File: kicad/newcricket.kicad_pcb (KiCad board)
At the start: 2 copper layers, 23 parts, among them IC11 ATTINY85-P, Q11 Q_NPN_BCE, SW11 SWITCH_INV, SW11 SW_PUSH, U11 78L05, U11 LM335

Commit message: A first version of the board and some changes to the schematic.
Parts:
- removed BT11 (x2): Battery, AAAAAGGHGGHGG:SMD_cr2032_holder
- removed C11: .01uF, Capacitors_SMD:C_1206_HandSoldering
- removed C11: 22uF, Capacitors_SMD:C_1210_HandSoldering
- removed C11: .01uF, Capacitors_SMD:C_1206
- removed D11: DIODE, Diodes_SMD:SOD-323
- removed IC11: ATTINY85-P, Housings_DIP:DIP-8_W7.62mm
- removed Q11: Q_NPN_BCE, TO_SOT_Packages_SMD:SOT-23_Handsoldering
- removed R11 (x5): 10k, Resistors_SMD:R_1206_HandSoldering
- removed R11: 1k, Resistors_SMD:R_1206_HandSoldering
- removed R11: LDR, AAAAAGGHGGHGG:LDR
- removed RV11 (x2): POT, bourns:BOURNS-3362P
- removed SP11: SPEAKER, Buzzers_Beepers:MagneticBuzzer_ProSignal_ABT-410-RC
- removed SW11 (x2): SW_PUSH, Buttons_Switches_SMD:SW_SPST_EVPBF
- removed SW11: SWITCH_INV, Buttons_Switches_SMD:SW_SPDT_PCM12
- removed U11: LM335, TO_SOT_Packages_THT:TO-92_Inline_Narrow_Oval
- removed U11: 78L05, AAAAAGGHGGHGG:78L05_handsoldering
- added BT1: Battery, aaevan_footprints:SMD_cr2032_holder, F.Cu at (91.9, 90.7)
- added BT2: Battery, aaevan_footprints:SMD_cr2032_holder, B.Cu at (91.9, 90.7)
- added C1: .01uF, Capacitors_SMD:C_1206_HandSoldering, B.Cu at (90.2, 76.0)
- added C2: 22uF, Capacitors_SMD:C_1210_HandSoldering, B.Cu at (87.3, 105.9)
- added C3: .01uF, Capacitors_SMD:C_1206_HandSoldering, B.Cu at (91.6, 69.0)
- added D1: DIODE, aaevan_footprints:SOD-323_handsoldering, B.Cu at (94.6, 108.5)
- added D2: D, aaevan_footprints:SOD-323_handsoldering, B.Cu at (99.9, 106.8)
- added D3: D, aaevan_footprints:SOD-323_handsoldering, B.Cu at (99.9, 110.9)
- added IC1: ATTINY85-P, Housings_DIP:DIP-8_W7.62mm, F.Cu at (87.8, 68.0)
- added Q1: Q_NPN_BCE, TO_SOT_Packages_SMD:SOT-23_Handsoldering, B.Cu at (94.6, 103.4)
- added R1: 10k, Resistors_SMD:R_1206_HandSoldering, B.Cu at (100.0, 75.3)
- added R2: 10k, Resistors_SMD:R_1206_HandSoldering, B.Cu at (83.2, 70.8)
- added R3: 10k, Resistors_SMD:R_1206_HandSoldering, B.Cu at (100.0, 71.0)
- added R4: 1k, Resistors_SMD:R_1206_HandSoldering, B.Cu at (83.2, 76.2)
- added R5: 10k, Resistors_SMD:R_1206_HandSoldering, B.Cu at (83.2, 73.5)
- added R6: LDR, aaevan_footprints:LDR, F.Cu at (104.1, 94.6)
- added R7: 10k, Resistors_SMD:R_1206_HandSoldering, B.Cu at (83.2, 68.1)
- added R8: JMP, Resistors_SMD:R_1206_HandSoldering, B.Cu at (95.0, 111.0)
- added RV1: POT, bourns:BOURNS-3362P, F.Cu at (101.2, 100.8)
- added RV2: POT, bourns:BOURNS-3362P, F.Cu at (82.1, 81.0)
- added SP1: SPEAKER, Buzzers_Beepers:MagneticBuzzer_ProSignal_ABT-410-RC, F.Cu at (97.8, 108.5)
- added SW1: SW_PUSH, Buttons_Switches_SMD:SW_SPST_EVPBF, F.Cu at (100.1, 71.9)
- added SW2: SW_PUSH, Buttons_Switches_SMD:SW_SPST_EVPBF, F.Cu at (85.1, 107.8)
- added SW3: SWITCH_INV, Buttons_Switches_SMD:SW_SPDT_PCM12, F.Cu at (103.7, 108.7)
- added U1: LM335, TO_SOT_Packages_THT:TO-92_Inline_Narrow_Oval, F.Cu at (80.6, 87.8)

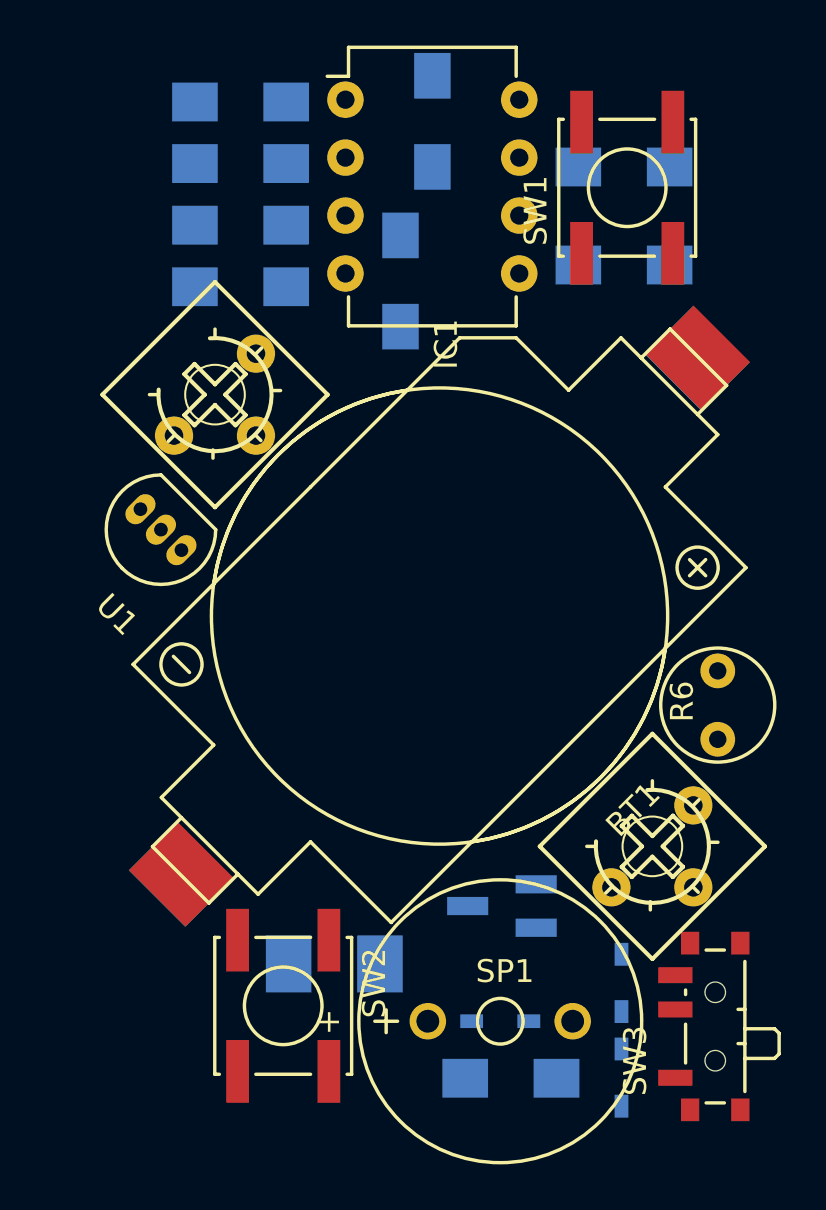
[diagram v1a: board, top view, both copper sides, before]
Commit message: Rearranged some components, soon to start laying traces.
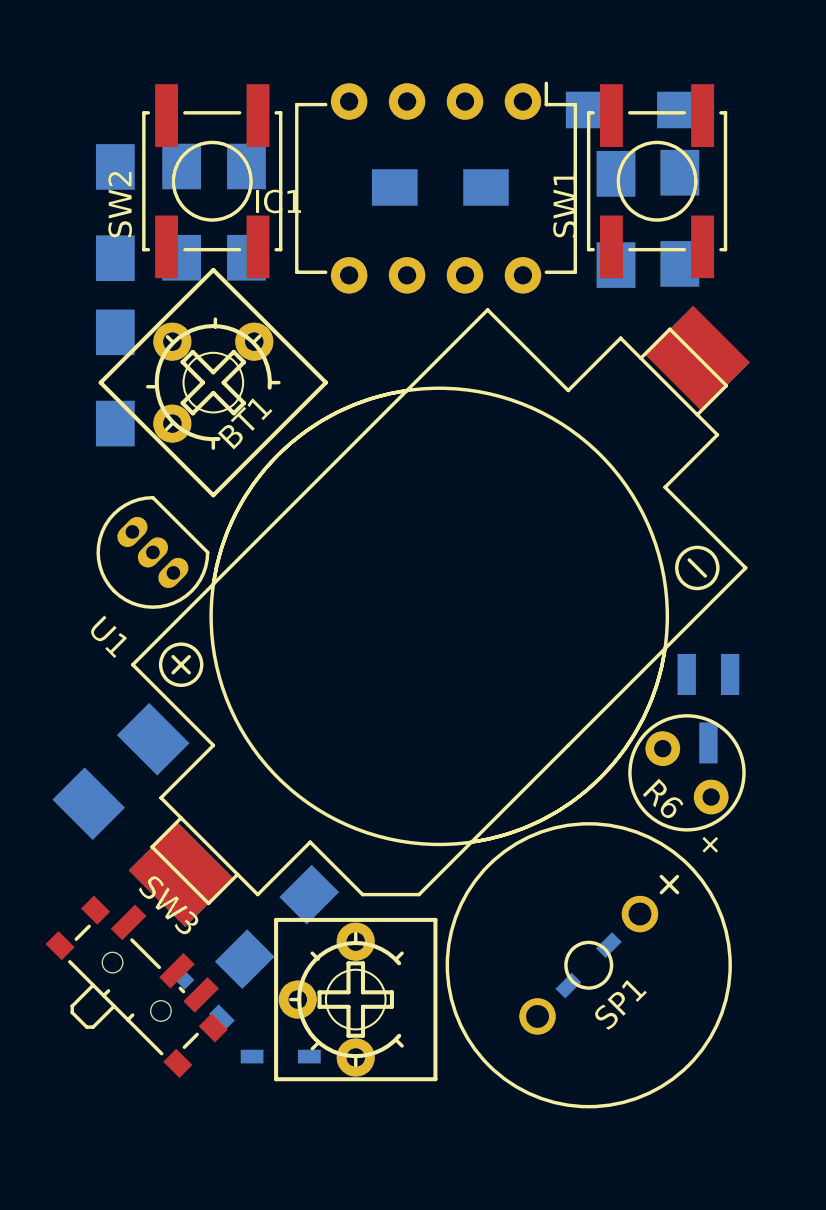
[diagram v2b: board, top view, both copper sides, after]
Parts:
- moved SW2 36.3 mm to (82.0, 71.6), turned to 90 degrees
- moved SW3 24.9 mm to (78.9, 106.7), turned to 315 degrees
- moved D2 18.4 mm to (81.5, 107.4), turned to 135 degrees
- moved D3 15.0 mm to (85.0, 110.0), turned to 180 degrees
- moved RV1 14.6 mm to (88.2, 107.5), turned to 90 degrees
- moved R7 13.3 mm to (77.7, 80.2), turned to 270 degrees
- moved C1 12.7 mm to (100.5, 68.5), turned to 0 degrees
- moved C2 12.6 mm to (78.0, 97.5), turned to 45 degrees
- moved Q1 12.5 mm to (103.7, 94.7), turned to 0 degrees
- moved R8 12.2 mm to (84.8, 104.3), turned to 225 degrees
- moved IC1 7.78 mm to (95.6, 68.1), turned to 270 degrees
- moved R2 5.89 mm to (77.7, 73.0), turned to 90 degrees
- moved D1 4.58 mm to (98.5, 106.0), turned to 45 degrees
- moved R3 3.33 mm to (102.5, 73.2), turned to 90 degrees
- moved R4 3.28 mm to (83.5, 73.0), turned to 90 degrees
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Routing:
- net (no net): track 0.00 -> 1.50 mm

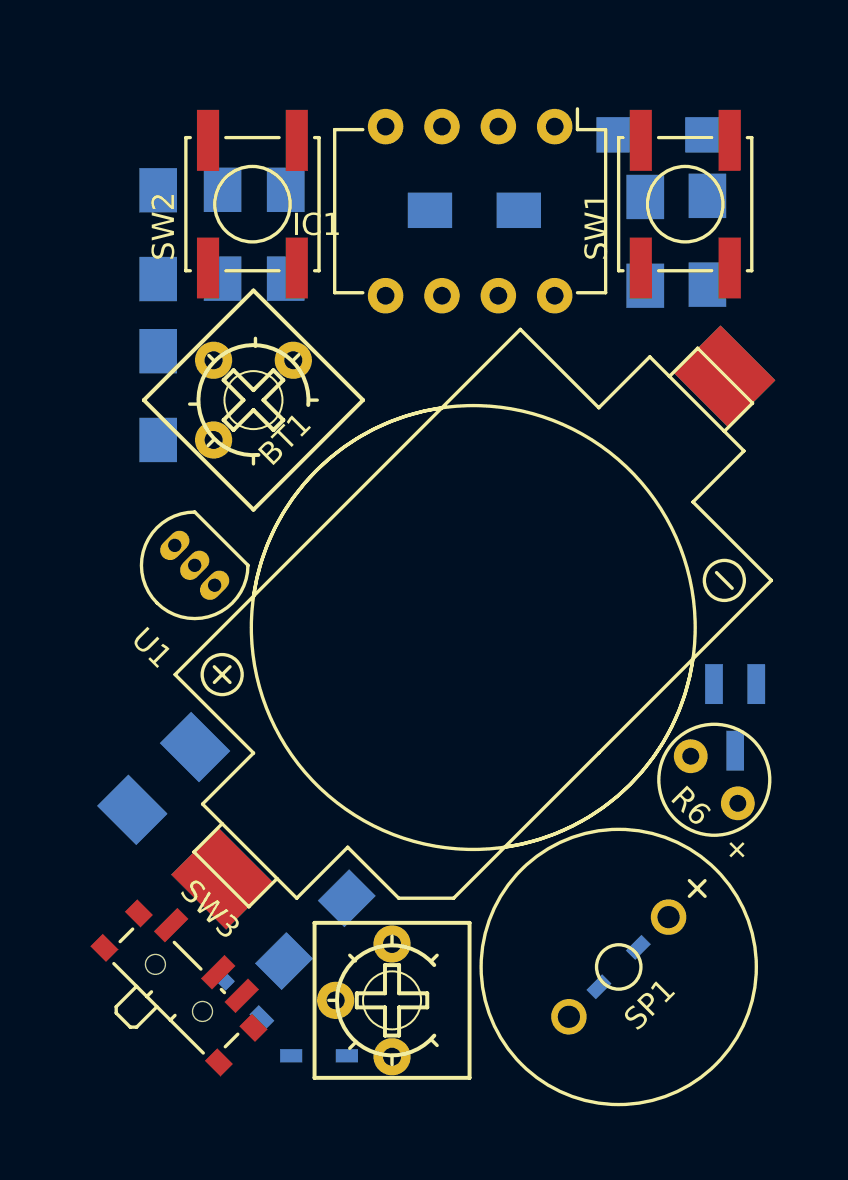
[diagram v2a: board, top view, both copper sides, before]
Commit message: Most of a layout-- still need to fix the switch so it's connected.
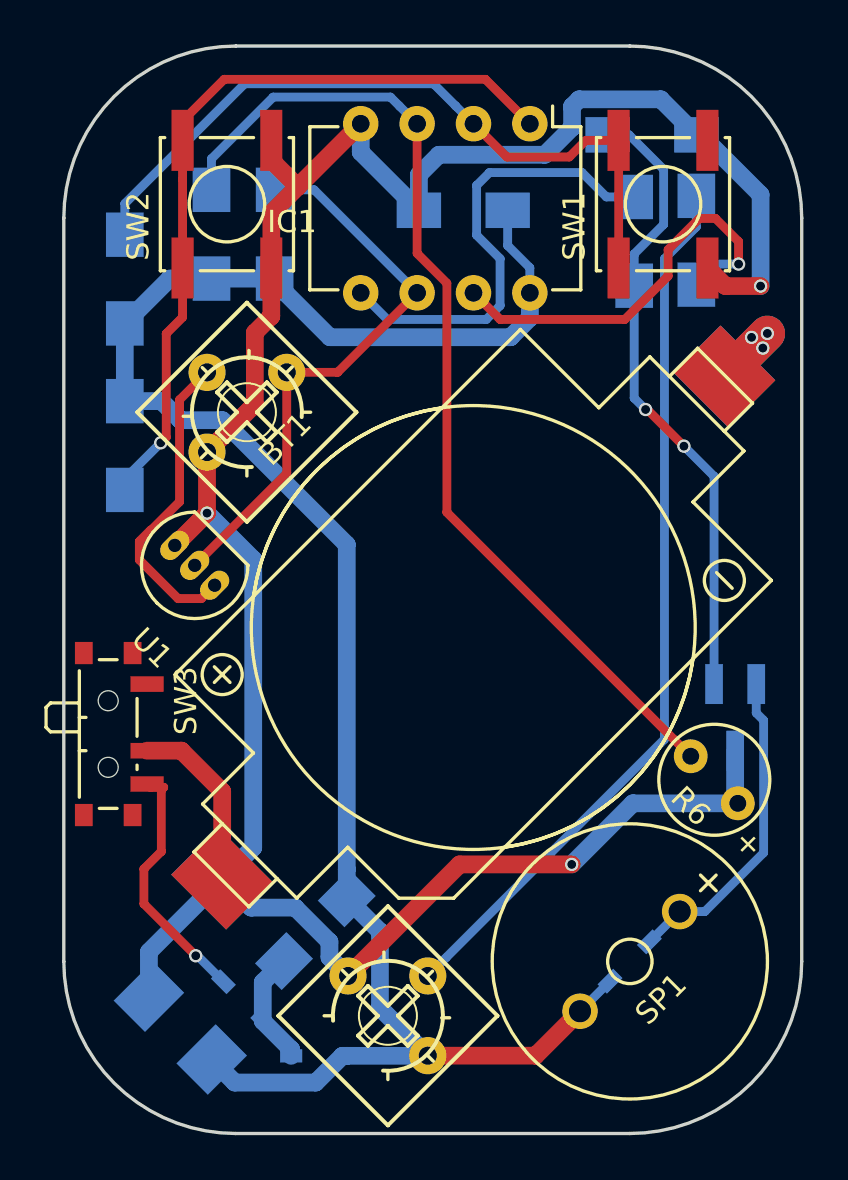
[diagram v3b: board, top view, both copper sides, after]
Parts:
- moved SW3 11.6 mm to (75.8, 95.5), turned to 270 degrees
- moved C2 11.3 mm to (78.7, 108.8), turned to 315 degrees
- moved R7 2.70 mm to (76.2, 82.5)
- moved R2 2.50 mm to (76.2, 75.0)
- moved SW2 1.15 mm to (80.8, 71.6)
- moved IC1 1.13 mm to (94.5, 68.0)
- moved SW1 1.00 mm to (100.5, 71.6)
- moved RV1 0.72 mm to (88.1, 108.2), turned to 315 degrees
- moved RV2 0.62 mm to (81.7, 81.0)
- moved D1 0.56 mm to (99.0, 105.8)
- moved SP1 0.56 mm to (96.7, 108.0)
- moved C1 0.50 mm to (100.0, 68.5)
- moved C3 0.50 mm to (91.5, 71.9)
- moved R1 0.50 mm to (99.2, 73.3)
- moved R3 0.50 mm to (102.0, 73.2)
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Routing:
- net GND: track 0.00 -> 114.2 mm, vias 0 -> 3
- net VCC: track 0.00 -> 86.9 mm
- net Net-(IC1-Pad3): track 0.00 -> 45.9 mm
- net Net-(R3-Pad2): track 0.00 -> 40.2 mm
- net Net-(IC1-Pad1): track 0.00 -> 35.0 mm, vias 0 -> 1
- net Net-(IC1-Pad2): track 0.00 -> 33.3 mm
- net Net-(C1-Pad1): track 0.00 -> 28.4 mm, vias 0 -> 2
- net Net-(IC1-Pad6): track 0.00 -> 26.1 mm
- net Net-(IC1-Pad5): track 0.00 -> 20.7 mm
- net Net-(IC1-Pad7): track 0.00 -> 18.8 mm, vias 0 -> 1
- net Net-(D1-Pad2): track 0.00 -> 14.5 mm
- net Net-(RV2-Pad2): track 0.00 -> 14.1 mm
- net Net-(D2-Pad2): track 0.00 -> 11.5 mm, vias 0 -> 1
- net Net-(BT1-Pad1): track 0.00 -> 8.07 mm
- net Net-(BT1-Pad2): track 0.00 -> 5.48 mm, vias 0 -> 1
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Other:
- board outline added: 33.2 x 49 mm

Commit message: Still throwing a few errors, filled zone placed. Board looking near-complete.
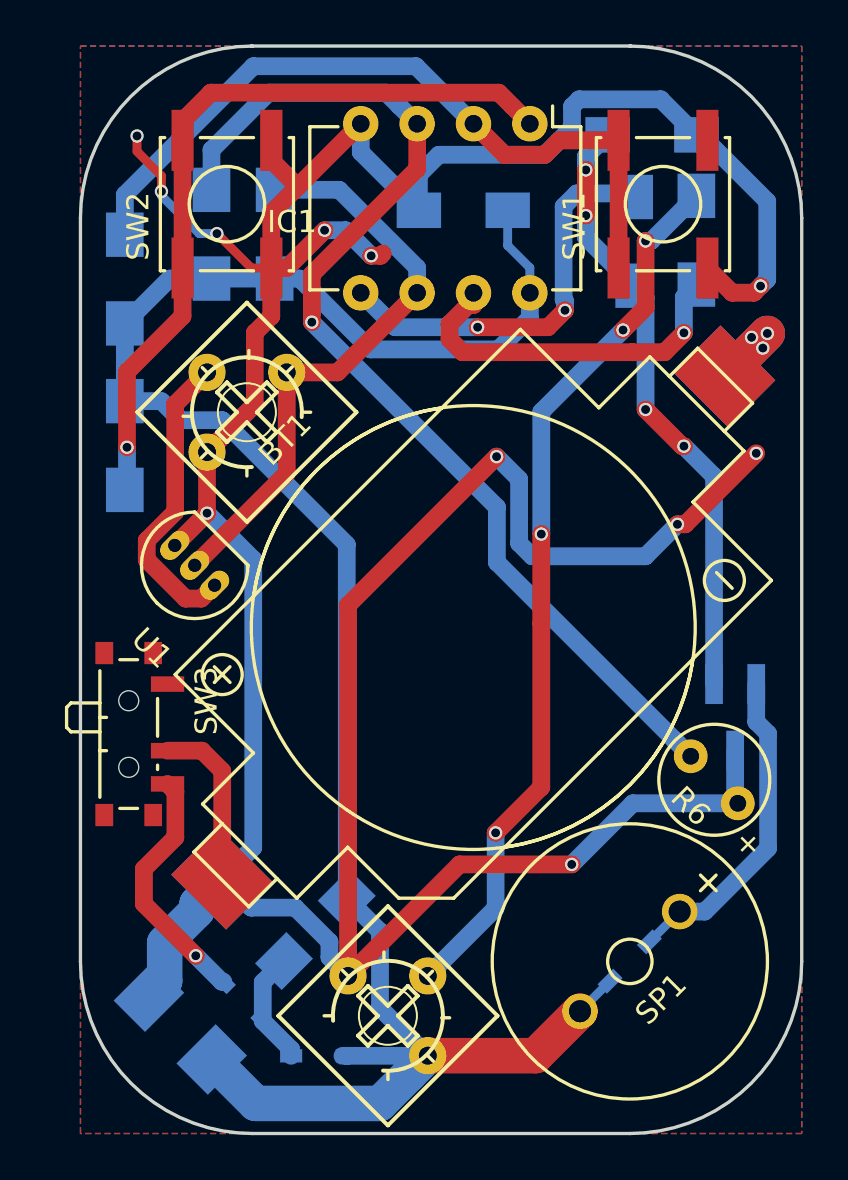
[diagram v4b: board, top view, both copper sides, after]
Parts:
- moved SW3 0.92 mm to (76.7, 95.5)
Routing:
- net GND: track 114.2 -> 173.8 mm, vias 3 -> 11
- net VCC: track 86.9 -> 91.9 mm
- net Net-(IC1-Pad3): track 45.9 -> 50.2 mm, vias 0 -> 2
- net Net-(IC1-Pad7): track 18.8 -> 16.2 mm
- net Net-(IC1-Pad1): track 35.0 -> 36.4 mm
- net Net-(R3-Pad2): track 40.2 -> 41.5 mm, vias 0 -> 4
- net Net-(C1-Pad1): track 28.4 -> 27.6 mm, vias 2 -> 4
- net Net-(IC1-Pad2): track 33.3 -> 34.1 mm
- net Net-(IC1-Pad6): track 26.1 -> 26.8 mm
- net Net-(IC1-Pad5): track 20.7 -> 20.0 mm, vias 0 -> 2
- added copper zone on B.Cu, net GND
- added copper zone on F.Cu, net GND
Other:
- board size 33.2 x 49 mm -> 32.5 x 49 mm

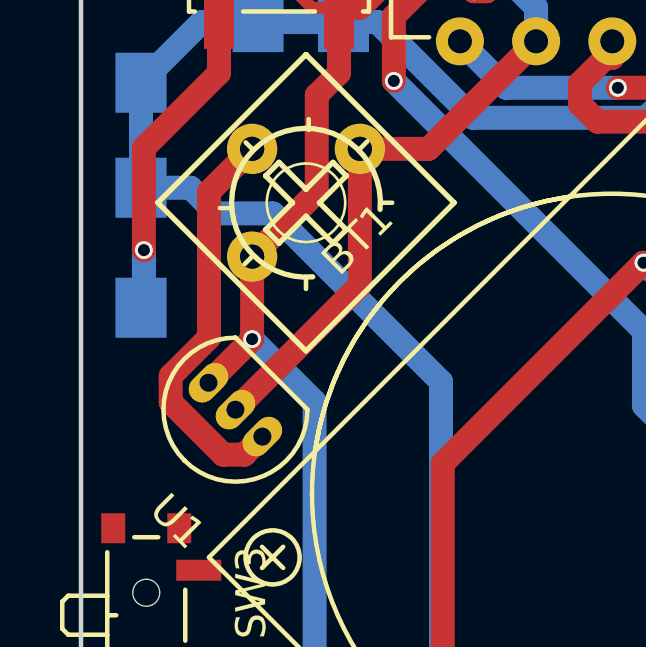
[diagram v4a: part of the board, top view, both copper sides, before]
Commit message: Fixed a pad clearance problem near the temperature sensor.
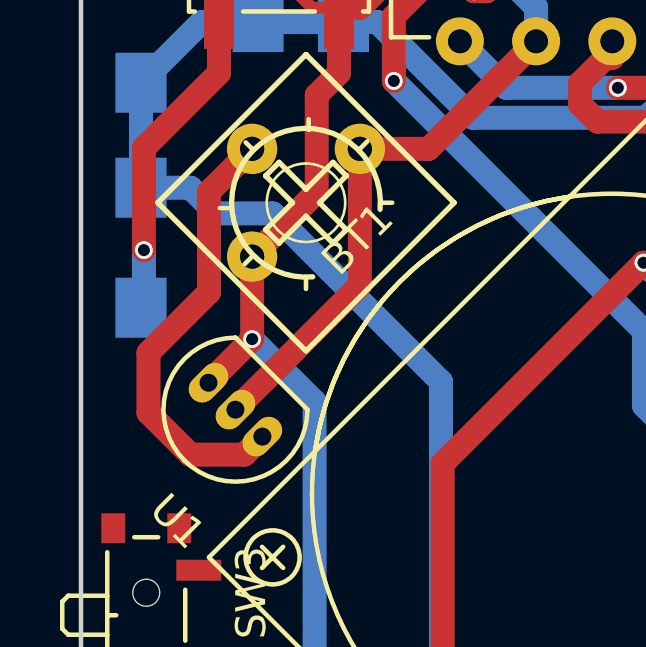
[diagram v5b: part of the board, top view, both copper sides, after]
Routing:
- net Net-(RV2-Pad2): track 13.6 -> 14.9 mm
- net Net-(BT1-Pad2): vias 1 -> 3
- net (no net): vias 2 -> 0
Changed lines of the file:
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@@
   (general
     (links 48)
-    (no_connects 4)
-    (area 73.837343 65.375 108.300001 114.263055)
+    (no_connects 0)
+    (area 74.124999 64.424999 106.775001 113.575001)
     (thickness 1.6)
     (drawings 8)
@@
   )
   (setup
-    (last_trace_width 0.4)
+    (last_trace_width 0.8)
     (user_trace_width 0.4)
     (user_trace_width 0.8)
@@
     (pad_drill 0.762)
     (pad_to_mask_clearance 0.2)
-    (aux_axis_origin 0 0)
-    (grid_origin 116.2 58.5)
+    (aux_axis_origin 74.2 113.5)
+    (grid_origin 74.2 113.5)
     (visible_elements FFFFFF7F)
     (pcbplotparams
@@
   (gr_arc (start 81.95 105.75) (end 81.95 113.5) (angle 90) (layer Edge.Cuts) (width 0.15))
   (gr_arc (start 98.95 105.75) (end 106.7 105.75) (angle 90) (layer Edge.Cuts) (width 0.15))
-  (via (at 104.9478 78.1088) (size 0.6) (drill 0.4) (layers F.Cu B.Cu) (net 0))
-  (via (at 104.4398 77.6262) (size 0.6) (drill 0.4) (layers F.Cu B.Cu) (net 0))
   (segment (start 81.2 68.75) (end 79.7 68.75) (width 0.25) (layer Dwgs.User) (net 0))
+  (via (at 104.9478 78.1088) (size 0.6) (drill 0.4) (layers F.Cu B.Cu) (net 1))
+  (via (at 104.4398 77.6262) (size 0.6) (drill 0.4) (layers F.Cu B.Cu) (net 1))
   (segment (start 103.213708 79.386292) (end 105.151 77.449) (width 1.6) (layer F.Cu) (net 1))
   (via (at 105.151 77.449) (size 0.6) (drill 0.4) (layers F.Cu B.Cu) (net 1))
@@
   (via (at 99.6646 73.2828) (size 0.6) (drill 0.4) (layers F.Cu B.Cu) (net 13))
   (segment (start 90.688199 105.561801) (end 89.85 106.4) (width 0.4) (layer B.Cu) (net 13))
+  (segment (start 77.847494 89.397494) (end 79.644608 89.397494) (width 0.8) (layer F.Cu) (net 14))
   (segment (start 79.644608 89.397494) (end 80.246051 88.796051) (width 0.8) (layer F.Cu) (net 14))
+  (segment (start 76.45 88) (end 77.847494 89.397494) (width 0.8) (layer F.Cu) (net 14))
+  (segment (start 76.45 86) (end 76.45 88) (width 0.8) (layer F.Cu) (net 14))
+  (segment (start 78.465748 83.984252) (end 76.45 86) (width 0.8) (layer F.Cu) (net 14))
+  (segment (start 78.465748 80.64215) (end 78.465748 83.984252) (width 0.8) (layer F.Cu) (net 14))
   (segment (start 79.903949 79.203949) (end 78.465748 80.64215) (width 0.8) (layer F.Cu) (net 14))
-  (segment (start 77.189289 86.776365) (end 77.189289 87.649299) (width 0.8) (layer F.Cu) (net 14))
-  (segment (start 78.465748 80.64215) (end 78.465748 85.499906) (width 0.8) (layer F.Cu) (net 14))
-  (segment (start 78.465748 85.499906) (end 77.189289 86.776365) (width 0.8) (layer F.Cu) (net 14))
-  (segment (start 77.189289 87.649299) (end 78.937484 89.397494) (width 0.8) (layer F.Cu) (net 14))
-  (segment (start 78.937484 89.397494) (end 79.644608 89.397494) (width 0.8) (layer F.Cu) (net 14))
   (segment (start 82.414838 108.433238) (end 82.414838 106.685162) (width 0.8) (layer B.Cu) (net 16))
   (segment (start 82.414838 106.685162) (end 83.371572 105.728428) (width 0.8) (layer B.Cu) (net 16))
